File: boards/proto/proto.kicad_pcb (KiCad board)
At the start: 2 copper layers, 100 x 100 mm, 5 parts, among them J1 XBUS_02, J2 PIA_INT, J3 VIA_INT, J4 ACIA_INT

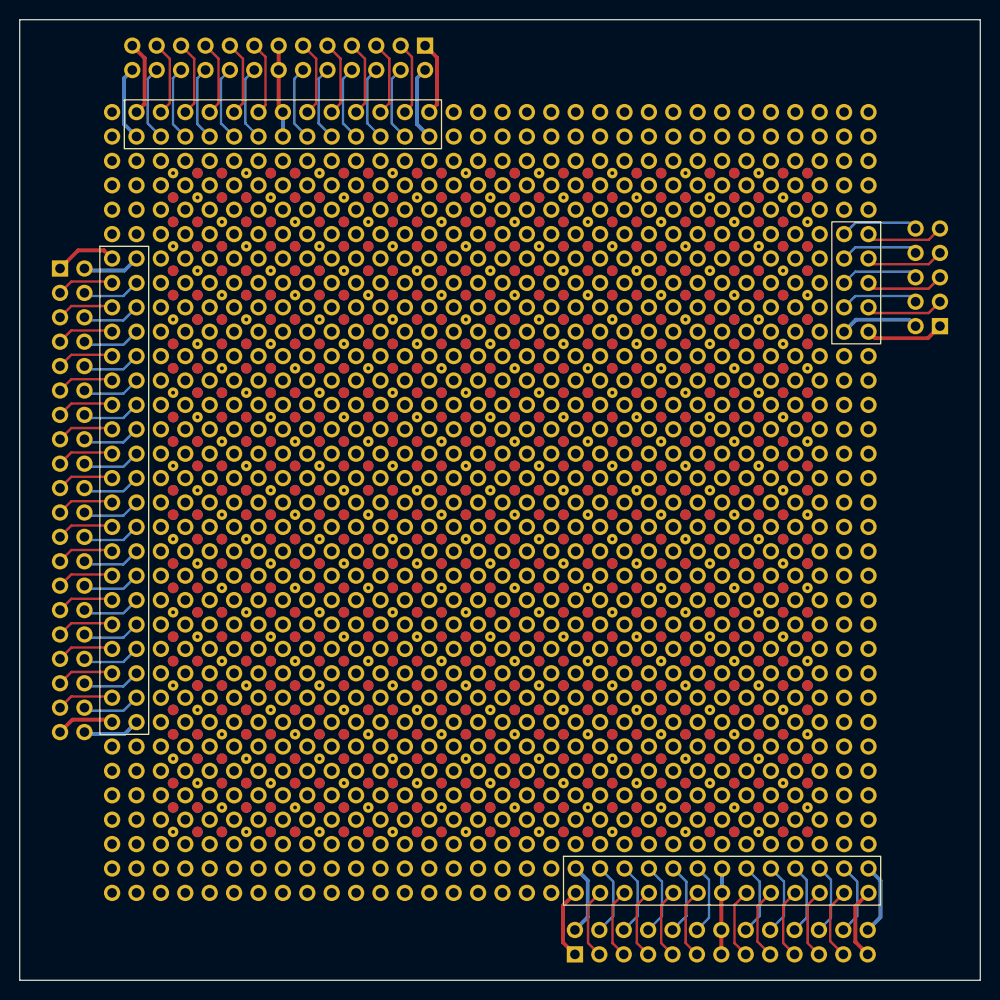
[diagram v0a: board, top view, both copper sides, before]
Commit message: Route PWR and GND traces from breakouts to proto rails.
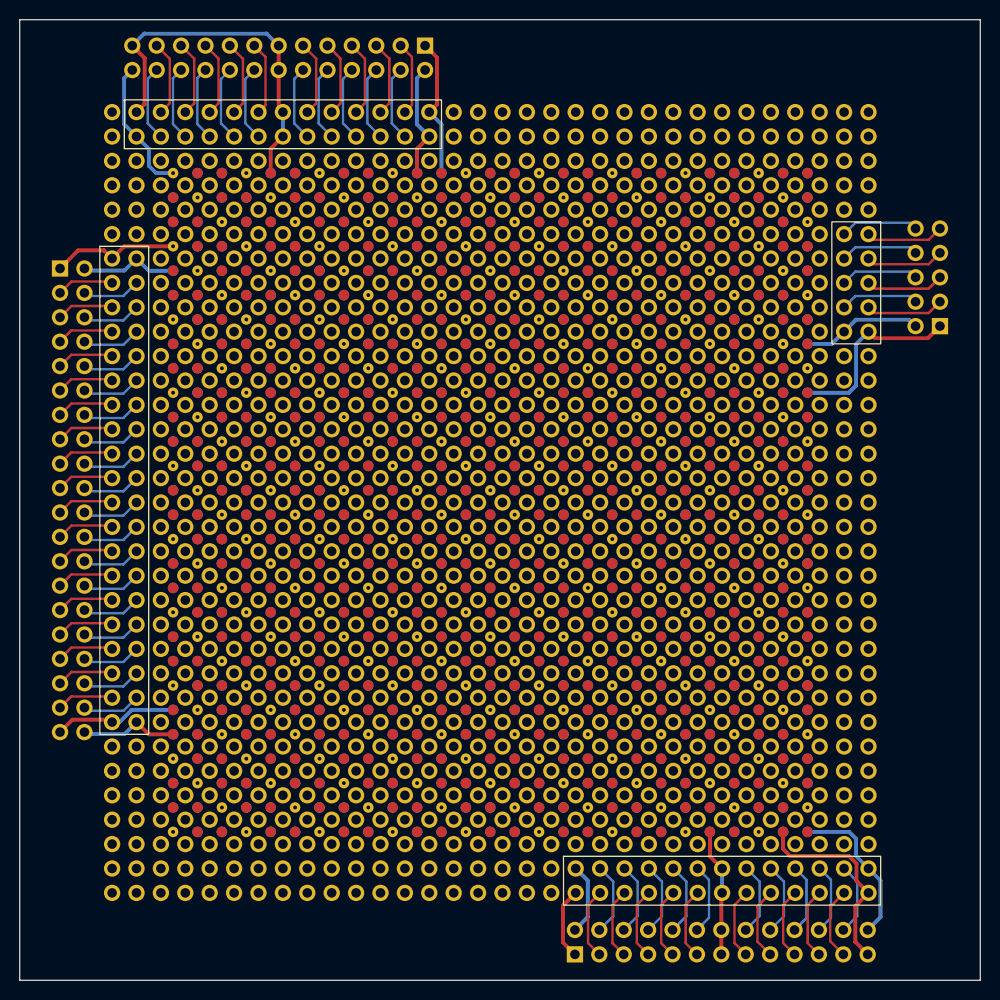
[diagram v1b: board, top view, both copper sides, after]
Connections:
- REF5 pad 1057: (no net) -> +5V
- REF5 pad 1058: (no net) -> +5V
- REF5 pad 1059: (no net) -> +5V
- REF5 pad 1060: (no net) -> +5V
- REF5 pad 1061: (no net) -> +5V
- REF5 pad 1062: (no net) -> +5V
- REF5 pad 1063: (no net) -> +5V
- REF5 pad 1064: (no net) -> +5V
- REF5 pad 1065: (no net) -> +5V
- REF5 pad 1066: (no net) -> +5V
- REF5 pad 1067: (no net) -> +5V
- REF5 pad 1068: (no net) -> +5V
- REF5 pad 1069: (no net) -> +5V
- REF5 pad 1070: (no net) -> +5V
- REF5 pad 1071: (no net) -> +5V
- REF5 pad 1072: (no net) -> +5V
- REF5 pad 1073: (no net) -> +5V
- REF5 pad 1074: (no net) -> +5V
- REF5 pad 1075: (no net) -> +5V
- REF5 pad 1076: (no net) -> +5V
- REF5 pad 1077: (no net) -> +5V
- REF5 pad 1078: (no net) -> +5V
- REF5 pad 1079: (no net) -> +5V
- REF5 pad 1080: (no net) -> +5V
- REF5 pad 1081: (no net) -> +5V
- REF5 pad 1082: (no net) -> +5V
- REF5 pad 1083: (no net) -> +5V
- REF5 pad 1084: (no net) -> +5V
- REF5 pad 1085: (no net) -> +5V
- REF5 pad 1086: (no net) -> +5V
- REF5 pad 1087: (no net) -> +5V
- REF5 pad 1088: (no net) -> +5V
- REF5 pad 1089: (no net) -> +5V
- REF5 pad 1090: (no net) -> +5V
- REF5 pad 1091: (no net) -> +5V
- REF5 pad 1092: (no net) -> +5V
- REF5 pad 1093: (no net) -> +5V
- REF5 pad 1094: (no net) -> +5V
- REF5 pad 1095: (no net) -> +5V
- REF5 pad 1096: (no net) -> +5V
- REF5 pad 1097: (no net) -> +5V
- REF5 pad 1098: (no net) -> +5V
- REF5 pad 1099: (no net) -> +5V
- REF5 pad 1100: (no net) -> +5V
- REF5 pad 1101: (no net) -> +5V
- REF5 pad 1102: (no net) -> +5V
- REF5 pad 1103: (no net) -> +5V
- REF5 pad 1104: (no net) -> +5V
- REF5 pad 1105: (no net) -> +5V
- REF5 pad 1106: (no net) -> +5V
- REF5 pad 1107: (no net) -> +5V
- REF5 pad 1108: (no net) -> +5V
- REF5 pad 1109: (no net) -> +5V
- REF5 pad 1110: (no net) -> +5V
- REF5 pad 1111: (no net) -> +5V
- REF5 pad 1112: (no net) -> +5V
- REF5 pad 1113: (no net) -> +5V
- REF5 pad 1114: (no net) -> +5V
- REF5 pad 1115: (no net) -> +5V
- REF5 pad 1116: (no net) -> +5V
- REF5 pad 1117: (no net) -> +5V
- REF5 pad 1118: (no net) -> +5V
- REF5 pad 1119: (no net) -> +5V
- REF5 pad 1120: (no net) -> +5V
- REF5 pad 1121: (no net) -> +5V
- REF5 pad 1122: (no net) -> +5V
- REF5 pad 1123: (no net) -> +5V
- REF5 pad 1124: (no net) -> +5V
- REF5 pad 1125: (no net) -> +5V
- REF5 pad 1126: (no net) -> +5V
- REF5 pad 1127: (no net) -> +5V
- REF5 pad 1128: (no net) -> +5V
- REF5 pad 1129: (no net) -> +5V
- REF5 pad 1130: (no net) -> +5V
- REF5 pad 1131: (no net) -> +5V
- REF5 pad 1132: (no net) -> +5V
- REF5 pad 1133: (no net) -> +5V
- REF5 pad 1134: (no net) -> +5V
- REF5 pad 1135: (no net) -> +5V
- REF5 pad 1136: (no net) -> +5V
- REF5 pad 1137: (no net) -> +5V
- REF5 pad 1138: (no net) -> +5V
- REF5 pad 1139: (no net) -> +5V
- REF5 pad 1140: (no net) -> +5V
- REF5 pad 1141: (no net) -> +5V
- REF5 pad 1142: (no net) -> +5V
- REF5 pad 1143: (no net) -> +5V
- REF5 pad 1144: (no net) -> +5V
- REF5 pad 1145: (no net) -> +5V
- REF5 pad 1146: (no net) -> +5V
- REF5 pad 1147: (no net) -> GND
- REF5 pad 1148: (no net) -> GND
- REF5 pad 1149: (no net) -> GND
- REF5 pad 1150: (no net) -> GND
- REF5 pad 1151: (no net) -> GND
- REF5 pad 1152: (no net) -> GND
- REF5 pad 1153: (no net) -> GND
- REF5 pad 1154: (no net) -> GND
- REF5 pad 1155: (no net) -> GND
- REF5 pad 1156: (no net) -> GND
- REF5 pad 1157: (no net) -> GND
- REF5 pad 1158: (no net) -> GND
- REF5 pad 1159: (no net) -> GND
- REF5 pad 1160: (no net) -> GND
- REF5 pad 1161: (no net) -> GND
- REF5 pad 1162: (no net) -> GND
- REF5 pad 1163: (no net) -> GND
- REF5 pad 1164: (no net) -> GND
- REF5 pad 1165: (no net) -> GND
- REF5 pad 1166: (no net) -> GND
- REF5 pad 1167: (no net) -> GND
- REF5 pad 1168: (no net) -> GND
- REF5 pad 1169: (no net) -> GND
- REF5 pad 1170: (no net) -> GND
- REF5 pad 1171: (no net) -> GND
- REF5 pad 1172: (no net) -> GND
- REF5 pad 1173: (no net) -> GND
- REF5 pad 1174: (no net) -> GND
- REF5 pad 1175: (no net) -> GND
- REF5 pad 1176: (no net) -> GND
- REF5 pad 1177: (no net) -> GND
- REF5 pad 1178: (no net) -> GND
- REF5 pad 1179: (no net) -> GND
- REF5 pad 1180: (no net) -> GND
- REF5 pad 1181: (no net) -> GND
- REF5 pad 1182: (no net) -> GND
- REF5 pad 1183: (no net) -> GND
- REF5 pad 1184: (no net) -> GND
- REF5 pad 1185: (no net) -> GND
- REF5 pad 1186: (no net) -> GND
- REF5 pad 1187: (no net) -> GND
- REF5 pad 1188: (no net) -> GND
- REF5 pad 1189: (no net) -> GND
- REF5 pad 1190: (no net) -> GND
- REF5 pad 1191: (no net) -> GND
- REF5 pad 1192: (no net) -> GND
- REF5 pad 1193: (no net) -> GND
- REF5 pad 1194: (no net) -> GND
- REF5 pad 1195: (no net) -> GND
- REF5 pad 1196: (no net) -> GND
- REF5 pad 1197: (no net) -> GND
- REF5 pad 1198: (no net) -> GND
- REF5 pad 1199: (no net) -> GND
- REF5 pad 1200: (no net) -> GND
- REF5 pad 1201: (no net) -> GND
- REF5 pad 1202: (no net) -> GND
- REF5 pad 1203: (no net) -> GND
- REF5 pad 1204: (no net) -> GND
- REF5 pad 1205: (no net) -> GND
- REF5 pad 1206: (no net) -> GND
- REF5 pad 1207: (no net) -> GND
- REF5 pad 1208: (no net) -> GND
- REF5 pad 1209: (no net) -> GND
- REF5 pad 1210: (no net) -> GND
- REF5 pad 1211: (no net) -> GND
- REF5 pad 1212: (no net) -> GND
- REF5 pad 1213: (no net) -> GND
- REF5 pad 1214: (no net) -> GND
- REF5 pad 1215: (no net) -> GND
- REF5 pad 1216: (no net) -> GND
- REF5 pad 1217: (no net) -> GND
- REF5 pad 1218: (no net) -> GND
- REF5 pad 1219: (no net) -> GND
- REF5 pad 1220: (no net) -> GND
- REF5 pad 1221: (no net) -> GND
- REF5 pad 1222: (no net) -> GND
- REF5 pad 1223: (no net) -> GND
- REF5 pad 1224: (no net) -> GND
- REF5 pad 1225: (no net) -> GND
- REF5 pad 1226: (no net) -> GND
- REF5 pad 1227: (no net) -> GND
- REF5 pad 1309: (no net) -> +5V
- REF5 pad 1310: (no net) -> +5V
- REF5 pad 1311: (no net) -> +5V
- REF5 pad 1312: (no net) -> +5V
- REF5 pad 1313: (no net) -> +5V
- REF5 pad 1314: (no net) -> +5V
- REF5 pad 1315: (no net) -> +5V
- REF5 pad 1316: (no net) -> +5V
- REF5 pad 1317: (no net) -> +5V
- REF5 pad 1318: (no net) -> +5V
- REF5 pad 1319: (no net) -> +5V
- REF5 pad 1320: (no net) -> +5V
- REF5 pad 1321: (no net) -> +5V
- REF5 pad 1322: (no net) -> +5V
- REF5 pad 1323: (no net) -> +5V
- REF5 pad 1324: (no net) -> +5V
- REF5 pad 1325: (no net) -> +5V
- REF5 pad 1326: (no net) -> +5V
- REF5 pad 1327: (no net) -> +5V
- REF5 pad 1328: (no net) -> +5V
- REF5 pad 1329: (no net) -> +5V
- REF5 pad 1330: (no net) -> +5V
- REF5 pad 1331: (no net) -> +5V
- REF5 pad 1332: (no net) -> +5V
- REF5 pad 1333: (no net) -> +5V
- REF5 pad 1334: (no net) -> +5V
- REF5 pad 1335: (no net) -> +5V
- REF5 pad 1336: (no net) -> +5V
- REF5 pad 1337: (no net) -> +5V
- REF5 pad 1338: (no net) -> +5V
- REF5 pad 1339: (no net) -> +5V
- REF5 pad 1340: (no net) -> +5V
- REF5 pad 1341: (no net) -> +5V
- REF5 pad 1342: (no net) -> +5V
- REF5 pad 1343: (no net) -> +5V
- REF5 pad 1344: (no net) -> +5V
- REF5 pad 1345: (no net) -> +5V
- REF5 pad 1346: (no net) -> +5V
- REF5 pad 1347: (no net) -> +5V
- REF5 pad 1348: (no net) -> +5V
- REF5 pad 1349: (no net) -> +5V
- REF5 pad 1350: (no net) -> +5V
- REF5 pad 1351: (no net) -> +5V
- REF5 pad 1352: (no net) -> +5V
- REF5 pad 1353: (no net) -> +5V
- REF5 pad 1354: (no net) -> +5V
- REF5 pad 1355: (no net) -> +5V
- REF5 pad 1356: (no net) -> +5V
- REF5 pad 1357: (no net) -> +5V
- REF5 pad 1358: (no net) -> +5V
- REF5 pad 1359: (no net) -> +5V
- REF5 pad 1360: (no net) -> +5V
- REF5 pad 1361: (no net) -> +5V
- REF5 pad 1362: (no net) -> +5V
- REF5 pad 1363: (no net) -> +5V
- REF5 pad 1364: (no net) -> +5V
- REF5 pad 1365: (no net) -> +5V
- REF5 pad 1366: (no net) -> +5V
- REF5 pad 1367: (no net) -> +5V
- REF5 pad 1368: (no net) -> +5V
- REF5 pad 1369: (no net) -> +5V
- REF5 pad 1370: (no net) -> +5V
- REF5 pad 1371: (no net) -> +5V
- REF5 pad 1372: (no net) -> +5V
- REF5 pad 1373: (no net) -> +5V
- REF5 pad 1374: (no net) -> +5V
- REF5 pad 1375: (no net) -> +5V
- REF5 pad 1376: (no net) -> +5V
- REF5 pad 1377: (no net) -> +5V
- REF5 pad 1378: (no net) -> +5V
- REF5 pad 1379: (no net) -> +5V
- REF5 pad 1380: (no net) -> +5V
- REF5 pad 1381: (no net) -> +5V
- REF5 pad 1382: (no net) -> +5V
- REF5 pad 1383: (no net) -> +5V
- REF5 pad 1384: (no net) -> +5V
- REF5 pad 1385: (no net) -> +5V
- REF5 pad 1386: (no net) -> +5V
- REF5 pad 1387: (no net) -> +5V
- REF5 pad 1388: (no net) -> +5V
- REF5 pad 1389: (no net) -> +5V
- REF5 pad 1390: (no net) -> +5V
- REF5 pad 1391: (no net) -> +5V
- REF5 pad 1392: (no net) -> +5V
- REF5 pad 1393: (no net) -> +5V
- REF5 pad 1394: (no net) -> +5V
- REF5 pad 1395: (no net) -> +5V
- REF5 pad 1396: (no net) -> +5V
- REF5 pad 1397: (no net) -> +5V
- REF5 pad 1398: (no net) -> +5V
- REF5 pad 1399: (no net) -> +5V
- REF5 pad 1400: (no net) -> +5V
- REF5 pad 1401: (no net) -> +5V
- REF5 pad 1402: (no net) -> +5V
- REF5 pad 1403: (no net) -> +5V
- REF5 pad 1404: (no net) -> +5V
- REF5 pad 1405: (no net) -> +5V
- REF5 pad 1406: (no net) -> +5V
- REF5 pad 1407: (no net) -> +5V
- REF5 pad 1408: (no net) -> +5V
- REF5 pad 1409: (no net) -> +5V
- REF5 pad 1410: (no net) -> +5V
- REF5 pad 1411: (no net) -> +5V
- REF5 pad 1412: (no net) -> +5V
- REF5 pad 1413: (no net) -> +5V
- REF5 pad 1414: (no net) -> +5V
- REF5 pad 1415: (no net) -> +5V
- REF5 pad 1416: (no net) -> +5V
- REF5 pad 1417: (no net) -> +5V
- REF5 pad 1418: (no net) -> +5V
- REF5 pad 1419: (no net) -> +5V
- REF5 pad 1420: (no net) -> +5V
- REF5 pad 1421: (no net) -> +5V
- REF5 pad 1422: (no net) -> +5V
- REF5 pad 1423: (no net) -> +5V
- REF5 pad 1424: (no net) -> +5V
- REF5 pad 1425: (no net) -> +5V
- REF5 pad 1426: (no net) -> +5V
- REF5 pad 1427: (no net) -> +5V
- REF5 pad 1428: (no net) -> +5V
- REF5 pad 1429: (no net) -> +5V
- REF5 pad 1430: (no net) -> +5V
- REF5 pad 1431: (no net) -> +5V
- REF5 pad 1432: (no net) -> +5V
- REF5 pad 1433: (no net) -> +5V
- REF5 pad 1434: (no net) -> +5V
- REF5 pad 1435: (no net) -> +5V
- REF5 pad 1436: (no net) -> +5V
- REF5 pad 1437: (no net) -> +5V
- REF5 pad 1438: (no net) -> +5V
- REF5 pad 1439: (no net) -> +5V
- REF5 pad 1440: (no net) -> +5V
- REF5 pad 1441: (no net) -> +5V
- REF5 pad 1442: (no net) -> +5V
- REF5 pad 1443: (no net) -> +5V
- REF5 pad 1444: (no net) -> +5V
- REF5 pad 1445: (no net) -> +5V
- REF5 pad 1446: (no net) -> +5V
- REF5 pad 1447: (no net) -> +5V
- REF5 pad 1448: (no net) -> +5V
- REF5 pad 1449: (no net) -> +5V
- REF5 pad 1450: (no net) -> +5V
- REF5 pad 1451: (no net) -> +5V
- REF5 pad 1452: (no net) -> +5V
- REF5 pad 1453: (no net) -> +5V
- REF5 pad 1454: (no net) -> +5V
- REF5 pad 1455: (no net) -> +5V
- REF5 pad 1456: (no net) -> +5V
- REF5 pad 1457: (no net) -> +5V
- REF5 pad 1458: (no net) -> +5V
- REF5 pad 1459: (no net) -> +5V
- REF5 pad 1460: (no net) -> +5V
- REF5 pad 1461: (no net) -> +5V
- REF5 pad 1462: (no net) -> +5V
- REF5 pad 1463: (no net) -> +5V
- REF5 pad 1464: (no net) -> +5V
- REF5 pad 1465: (no net) -> +5V
- REF5 pad 1466: (no net) -> +5V
- REF5 pad 1467: (no net) -> +5V
- REF5 pad 1468: (no net) -> +5V
- REF5 pad 1469: (no net) -> +5V
- REF5 pad 1470: (no net) -> +5V
- REF5 pad 1471: (no net) -> +5V
- REF5 pad 1472: (no net) -> +5V
- REF5 pad 1473: (no net) -> +5V
- REF5 pad 1474: (no net) -> +5V
- REF5 pad 1475: (no net) -> +5V
- REF5 pad 1476: (no net) -> +5V
- REF5 pad 1477: (no net) -> +5V
- REF5 pad 1478: (no net) -> +5V
- REF5 pad 1479: (no net) -> +5V
- REF5 pad 1480: (no net) -> +5V
- REF5 pad 1481: (no net) -> +5V
- REF5 pad 1482: (no net) -> +5V
- REF5 pad 1483: (no net) -> +5V
- REF5 pad 1484: (no net) -> +5V
- REF5 pad 1485: (no net) -> +5V
- REF5 pad 1486: (no net) -> +5V
- REF5 pad 1487: (no net) -> +5V
- REF5 pad 1488: (no net) -> +5V
- REF5 pad 1489: (no net) -> +5V
- REF5 pad 1490: (no net) -> +5V
- REF5 pad 1491: (no net) -> +5V
- REF5 pad 1492: (no net) -> +5V
- REF5 pad 1493: (no net) -> +5V
- REF5 pad 1494: (no net) -> +5V
- REF5 pad 1495: (no net) -> +5V
- REF5 pad 1496: (no net) -> +5V
- REF5 pad 1497: (no net) -> +5V
- REF5 pad 1498: (no net) -> +5V
- REF5 pad 1499: (no net) -> +5V
- REF5 pad 1500: (no net) -> +5V
- REF5 pad 1501: (no net) -> +5V
- REF5 pad 1502: (no net) -> +5V
- REF5 pad 1503: (no net) -> +5V
- REF5 pad 1504: (no net) -> +5V
- REF5 pad 1505: (no net) -> +5V
- REF5 pad 1506: (no net) -> +5V
- REF5 pad 1507: (no net) -> +5V
- REF5 pad 1508: (no net) -> +5V
- REF5 pad 1509: (no net) -> +5V
- REF5 pad 1510: (no net) -> +5V
- REF5 pad 1511: (no net) -> +5V
- REF5 pad 1512: (no net) -> +5V
- REF5 pad 1513: (no net) -> +5V
- REF5 pad 1514: (no net) -> +5V
- REF5 pad 1515: (no net) -> +5V
- REF5 pad 1516: (no net) -> +5V
- REF5 pad 1517: (no net) -> +5V
- REF5 pad 1518: (no net) -> +5V
- REF5 pad 1519: (no net) -> +5V
- REF5 pad 1520: (no net) -> +5V
- REF5 pad 1521: (no net) -> +5V
- REF5 pad 1522: (no net) -> +5V
- REF5 pad 1523: (no net) -> +5V
- REF5 pad 1524: (no net) -> +5V
- REF5 pad 1525: (no net) -> +5V
- REF5 pad 1526: (no net) -> +5V
- REF5 pad 1527: (no net) -> +5V
- REF5 pad 1528: (no net) -> +5V
- REF5 pad 1529: (no net) -> +5V
- REF5 pad 1530: (no net) -> +5V
- REF5 pad 1531: (no net) -> +5V
- REF5 pad 1532: (no net) -> +5V
- REF5 pad 1533: (no net) -> +5V
- REF5 pad 1534: (no net) -> +5V
- REF5 pad 1535: (no net) -> +5V
- REF5 pad 1536: (no net) -> +5V
- REF5 pad 1537: (no net) -> +5V
- REF5 pad 1538: (no net) -> +5V
- REF5 pad 1539: (no net) -> +5V
- REF5 pad 1540: (no net) -> +5V
- REF5 pad 1541: (no net) -> +5V
- REF5 pad 1542: (no net) -> +5V
- REF5 pad 1543: (no net) -> +5V
- REF5 pad 1544: (no net) -> +5V
- REF5 pad 1545: (no net) -> +5V
- REF5 pad 1546: (no net) -> +5V
- REF5 pad 1547: (no net) -> +5V
- REF5 pad 1548: (no net) -> +5V
- REF5 pad 1549: (no net) -> +5V
- REF5 pad 1550: (no net) -> +5V
- REF5 pad 1551: (no net) -> +5V
- REF5 pad 1552: (no net) -> +5V
- REF5 pad 1553: (no net) -> +5V
- REF5 pad 1554: (no net) -> +5V
- REF5 pad 1555: (no net) -> +5V
- REF5 pad 1556: (no net) -> +5V
- REF5 pad 1557: (no net) -> +5V
- REF5 pad 1558: (no net) -> +5V
- REF5 pad 1559: (no net) -> +5V
- REF5 pad 1560: (no net) -> +5V
- REF5 pad 1561: (no net) -> +5V
- REF5 pad 1562: (no net) -> +5V
- REF5 pad 1563: (no net) -> +5V
- REF5 pad 1564: (no net) -> +5V
- REF5 pad 1565: (no net) -> +5V
- REF5 pad 1566: (no net) -> +5V
- REF5 pad 1567: (no net) -> +5V
- REF5 pad 1568: (no net) -> +5V
- REF5 pad 1569: (no net) -> +5V
- REF5 pad 1570: (no net) -> +5V
- REF5 pad 1571: (no net) -> +5V
- REF5 pad 1572: (no net) -> +5V
- REF5 pad 1573: (no net) -> +5V
- REF5 pad 1574: (no net) -> +5V
- REF5 pad 1575: (no net) -> +5V
- REF5 pad 1576: (no net) -> +5V
- REF5 pad 1577: (no net) -> +5V
- REF5 pad 1578: (no net) -> +5V
- REF5 pad 1579: (no net) -> +5V
- REF5 pad 1580: (no net) -> +5V
- REF5 pad 1581: (no net) -> +5V
- REF5 pad 1582: (no net) -> +5V
- REF5 pad 1583: (no net) -> +5V
- REF5 pad 1584: (no net) -> +5V
- REF5 pad 1585: (no net) -> +5V
- REF5 pad 1586: (no net) -> +5V
- REF5 pad 1587: (no net) -> +5V
- REF5 pad 1588: (no net) -> +5V
- REF5 pad 1589: (no net) -> +5V
- REF5 pad 1590: (no net) -> +5V
- REF5 pad 1591: (no net) -> +5V
- REF5 pad 1592: (no net) -> +5V
- REF5 pad 1593: (no net) -> +5V
- REF5 pad 1594: (no net) -> +5V
- REF5 pad 1595: (no net) -> +5V
- REF5 pad 1596: (no net) -> +5V
- REF5 pad 1597: (no net) -> +5V
- REF5 pad 1598: (no net) -> +5V
- REF5 pad 1599: (no net) -> +5V
- REF5 pad 1600: (no net) -> +5V
- REF5 pad 1601: (no net) -> +5V
- REF5 pad 1602: (no net) -> +5V
- REF5 pad 1603: (no net) -> +5V
- REF5 pad 1604: (no net) -> +5V
- REF5 pad 1605: (no net) -> +5V
- REF5 pad 1606: (no net) -> +5V
- REF5 pad 1607: (no net) -> +5V
- REF5 pad 1608: (no net) -> +5V
- REF5 pad 1609: (no net) -> +5V
- REF5 pad 1610: (no net) -> +5V
- REF5 pad 1611: (no net) -> +5V
- REF5 pad 1612: (no net) -> +5V
- REF5 pad 1613: (no net) -> +5V
- REF5 pad 1614: (no net) -> +5V
- REF5 pad 1615: (no net) -> +5V
- REF5 pad 1616: (no net) -> +5V
- REF5 pad 1617: (no net) -> +5V
- REF5 pad 1618: (no net) -> +5V
- REF5 pad 1619: (no net) -> +5V
- REF5 pad 1620: (no net) -> +5V
- REF5 pad 1621: (no net) -> +5V
- REF5 pad 1622: (no net) -> +5V
- REF5 pad 1623: (no net) -> +5V
- REF5 pad 1624: (no net) -> +5V
- REF5 pad 1625: (no net) -> +5V
- REF5 pad 1626: (no net) -> +5V
- REF5 pad 1627: (no net) -> +5V
- REF5 pad 1628: (no net) -> +5V
- REF5 pad 1629: (no net) -> +5V
- REF5 pad 1630: (no net) -> +5V
- REF5 pad 1631: (no net) -> +5V
- REF5 pad 1632: (no net) -> +5V
- REF5 pad 1633: (no net) -> +5V
- REF5 pad 1634: (no net) -> +5V
- REF5 pad 1635: (no net) -> +5V
- REF5 pad 1636: (no net) -> +5V
- REF5 pad 1637: (no net) -> +5V
- REF5 pad 1638: (no net) -> +5V
- REF5 pad 1639: (no net) -> +5V
- REF5 pad 1640: (no net) -> +5V
- REF5 pad 1641: (no net) -> +5V
- REF5 pad 1642: (no net) -> +5V
- REF5 pad 1643: (no net) -> +5V
- REF5 pad 1644: (no net) -> +5V
- REF5 pad 1645: (no net) -> +5V
- REF5 pad 1646: (no net) -> +5V
- REF5 pad 1647: (no net) -> +5V
- REF5 pad 1648: (no net) -> +5V
- REF5 pad 1649: (no net) -> +5V
- REF5 pad 1650: (no net) -> +5V
- REF5 pad 1651: (no net) -> GND
- REF5 pad 1652: (no net) -> GND
- REF5 pad 1653: (no net) -> GND
- REF5 pad 1654: (no net) -> GND
- REF5 pad 1655: (no net) -> GND
- REF5 pad 1656: (no net) -> GND
- REF5 pad 1657: (no net) -> GND
- REF5 pad 1658: (no net) -> GND
- REF5 pad 1659: (no net) -> GND
- REF5 pad 1660: (no net) -> GND
- REF5 pad 1661: (no net) -> GND
- REF5 pad 1662: (no net) -> GND
- REF5 pad 1663: (no net) -> GND
- REF5 pad 1664: (no net) -> GND
- REF5 pad 1665: (no net) -> GND
- REF5 pad 1666: (no net) -> GND
- REF5 pad 1667: (no net) -> GND
- REF5 pad 1668: (no net) -> GND
- REF5 pad 1669: (no net) -> GND
- REF5 pad 1670: (no net) -> GND
- REF5 pad 1671: (no net) -> GND
- REF5 pad 1672: (no net) -> GND
- REF5 pad 1673: (no net) -> GND
- REF5 pad 1674: (no net) -> GND
- REF5 pad 1675: (no net) -> GND
- REF5 pad 1676: (no net) -> GND
- REF5 pad 1677: (no net) -> GND
- REF5 pad 1678: (no net) -> GND
- REF5 pad 1679: (no net) -> GND
- REF5 pad 1680: (no net) -> GND
- REF5 pad 1681: (no net) -> GND
- REF5 pad 1682: (no net) -> GND
- REF5 pad 1683: (no net) -> GND
- REF5 pad 1684: (no net) -> GND
- REF5 pad 1685: (no net) -> GND
- REF5 pad 1686: (no net) -> GND
- REF5 pad 1687: (no net) -> GND
- REF5 pad 1688: (no net) -> GND
- REF5 pad 1689: (no net) -> GND
- REF5 pad 1690: (no net) -> GND
- REF5 pad 1691: (no net) -> GND
- REF5 pad 1692: (no net) -> GND
- REF5 pad 1693: (no net) -> GND
- REF5 pad 1694: (no net) -> GND
- REF5 pad 1695: (no net) -> GND
- REF5 pad 1696: (no net) -> GND
- REF5 pad 1697: (no net) -> GND
- REF5 pad 1698: (no net) -> GND
- REF5 pad 1699: (no net) -> GND
- REF5 pad 1700: (no net) -> GND
- REF5 pad 1701: (no net) -> GND
- REF5 pad 1702: (no net) -> GND
- REF5 pad 1703: (no net) -> GND
- REF5 pad 1704: (no net) -> GND
- REF5 pad 1705: (no net) -> GND
- REF5 pad 1706: (no net) -> GND
- REF5 pad 1707: (no net) -> GND
- REF5 pad 1708: (no net) -> GND
- REF5 pad 1709: (no net) -> GND
- REF5 pad 1710: (no net) -> GND
- REF5 pad 1711: (no net) -> GND
- REF5 pad 1712: (no net) -> GND
- REF5 pad 1713: (no net) -> GND
- REF5 pad 1714: (no net) -> GND
- REF5 pad 1715: (no net) -> GND
- REF5 pad 1716: (no net) -> GND
- REF5 pad 1717: (no net) -> GND
- REF5 pad 1718: (no net) -> GND
- REF5 pad 1719: (no net) -> GND
- REF5 pad 1720: (no net) -> GND
- REF5 pad 1721: (no net) -> GND
- REF5 pad 1722: (no net) -> GND
- REF5 pad 1723: (no net) -> GND
- REF5 pad 1724: (no net) -> GND
- REF5 pad 1725: (no net) -> GND
- REF5 pad 1726: (no net) -> GND
- REF5 pad 1727: (no net) -> GND
- REF5 pad 1728: (no net) -> GND
- REF5 pad 1729: (no net) -> GND
- REF5 pad 1730: (no net) -> GND
- REF5 pad 1731: (no net) -> GND
- REF5 pad 1732: (no net) -> GND
- REF5 pad 1733: (no net) -> GND
- REF5 pad 1734: (no net) -> GND
- REF5 pad 1735: (no net) -> GND
- REF5 pad 1736: (no net) -> GND
- REF5 pad 1737: (no net) -> GND
- REF5 pad 1738: (no net) -> GND
- REF5 pad 1739: (no net) -> GND
- REF5 pad 1740: (no net) -> GND
- REF5 pad 1741: (no net) -> GND
- REF5 pad 1742: (no net) -> GND
- REF5 pad 1743: (no net) -> GND
- REF5 pad 1744: (no net) -> GND
- REF5 pad 1745: (no net) -> GND
- REF5 pad 1746: (no net) -> GND
- REF5 pad 1747: (no net) -> GND
- REF5 pad 1748: (no net) -> GND
- REF5 pad 1749: (no net) -> GND
- REF5 pad 1750: (no net) -> GND
- REF5 pad 1751: (no net) -> GND
- REF5 pad 1752: (no net) -> GND
- REF5 pad 1753: (no net) -> GND
- REF5 pad 1754: (no net) -> GND
- REF5 pad 1755: (no net) -> GND
- REF5 pad 1756: (no net) -> GND
- REF5 pad 1757: (no net) -> GND
- REF5 pad 1758: (no net) -> GND
- REF5 pad 1759: (no net) -> GND
- REF5 pad 1760: (no net) -> GND
- REF5 pad 1761: (no net) -> GND
- REF5 pad 1762: (no net) -> GND
- REF5 pad 1763: (no net) -> GND
- REF5 pad 1764: (no net) -> GND
- REF5 pad 1765: (no net) -> GND
- REF5 pad 1766: (no net) -> GND
- REF5 pad 1767: (no net) -> GND
- REF5 pad 1768: (no net) -> GND
- REF5 pad 1769: (no net) -> GND
- REF5 pad 1770: (no net) -> GND
- REF5 pad 1771: (no net) -> GND
- REF5 pad 1772: (no net) -> GND
- REF5 pad 1773: (no net) -> GND
- REF5 pad 1774: (no net) -> GND
- REF5 pad 1775: (no net) -> GND
- REF5 pad 1776: (no net) -> GND
- REF5 pad 1777: (no net) -> GND
- REF5 pad 1778: (no net) -> GND
- REF5 pad 1779: (no net) -> GND
- REF5 pad 1780: (no net) -> GND
- REF5 pad 1781: (no net) -> GND
- REF5 pad 1782: (no net) -> GND
- REF5 pad 1783: (no net) -> GND
- REF5 pad 1784: (no net) -> GND
- REF5 pad 1785: (no net) -> GND
- REF5 pad 1786: (no net) -> GND
- REF5 pad 1787: (no net) -> GND
- REF5 pad 1788: (no net) -> GND
- REF5 pad 1789: (no net) -> GND
- REF5 pad 1790: (no net) -> GND
- REF5 pad 1791: (no net) -> GND
- REF5 pad 1792: (no net) -> GND
- REF5 pad 1793: (no net) -> GND
- REF5 pad 1794: (no net) -> GND
- REF5 pad 1795: (no net) -> GND
- REF5 pad 1796: (no net) -> GND
- REF5 pad 1797: (no net) -> GND
- REF5 pad 1798: (no net) -> GND
- REF5 pad 1799: (no net) -> GND
- REF5 pad 1800: (no net) -> GND
- REF5 pad 1801: (no net) -> GND
- REF5 pad 1802: (no net) -> GND
- REF5 pad 1803: (no net) -> GND
- REF5 pad 1804: (no net) -> GND
- REF5 pad 1805: (no net) -> GND
- REF5 pad 1806: (no net) -> GND
- REF5 pad 1807: (no net) -> GND
- REF5 pad 1808: (no net) -> GND
- REF5 pad 1809: (no net) -> GND
- REF5 pad 1810: (no net) -> GND
- REF5 pad 1811: (no net) -> GND
- REF5 pad 1812: (no net) -> GND
- REF5 pad 1813: (no net) -> GND
- REF5 pad 1814: (no net) -> GND
- REF5 pad 1815: (no net) -> GND
- REF5 pad 1816: (no net) -> GND
- REF5 pad 1817: (no net) -> GND
- REF5 pad 1818: (no net) -> GND
- REF5 pad 1819: (no net) -> GND
- REF5 pad 1820: (no net) -> GND
- REF5 pad 1821: (no net) -> GND
- REF5 pad 1822: (no net) -> GND
- REF5 pad 1823: (no net) -> GND
- REF5 pad 1824: (no net) -> GND
- REF5 pad 1825: (no net) -> GND
- REF5 pad 1826: (no net) -> GND
- REF5 pad 1827: (no net) -> GND
- REF5 pad 1828: (no net) -> GND
- REF5 pad 1829: (no net) -> GND
- REF5 pad 1830: (no net) -> GND
- REF5 pad 1831: (no net) -> GND
- REF5 pad 1832: (no net) -> GND
- REF5 pad 1833: (no net) -> GND
- REF5 pad 1834: (no net) -> GND
- REF5 pad 1835: (no net) -> GND
- REF5 pad 1836: (no net) -> GND
- REF5 pad 1837: (no net) -> GND
- REF5 pad 1838: (no net) -> GND
- REF5 pad 1839: (no net) -> GND
- REF5 pad 1840: (no net) -> GND
- REF5 pad 1841: (no net) -> GND
- REF5 pad 1842: (no net) -> GND
- REF5 pad 1843: (no net) -> GND
- REF5 pad 1844: (no net) -> GND
- REF5 pad 1845: (no net) -> GND
- REF5 pad 1846: (no net) -> GND
- REF5 pad 1847: (no net) -> GND
- REF5 pad 1848: (no net) -> GND
- REF5 pad 1849: (no net) -> GND
- REF5 pad 1850: (no net) -> GND
- REF5 pad 1851: (no net) -> GND
- REF5 pad 1852: (no net) -> GND
- REF5 pad 1853: (no net) -> GND
- REF5 pad 1854: (no net) -> GND
- REF5 pad 1855: (no net) -> GND
- REF5 pad 1856: (no net) -> GND
- REF5 pad 1857: (no net) -> GND
- REF5 pad 1858: (no net) -> GND
- REF5 pad 1859: (no net) -> GND
- REF5 pad 1860: (no net) -> GND
- REF5 pad 1861: (no net) -> GND
- REF5 pad 1862: (no net) -> GND
- REF5 pad 1863: (no net) -> GND
- REF5 pad 1864: (no net) -> GND
- REF5 pad 1865: (no net) -> GND
- REF5 pad 1866: (no net) -> GND
- REF5 pad 1867: (no net) -> GND
- REF5 pad 1868: (no net) -> GND
- REF5 pad 1869: (no net) -> GND
- REF5 pad 1870: (no net) -> GND
- REF5 pad 1871: (no net) -> GND
- REF5 pad 1872: (no net) -> GND
- REF5 pad 1873: (no net) -> GND
- REF5 pad 1874: (no net) -> GND
- REF5 pad 1875: (no net) -> GND
- REF5 pad 1876: (no net) -> GND
- REF5 pad 1877: (no net) -> GND
- REF5 pad 1878: (no net) -> GND
- REF5 pad 1879: (no net) -> GND
- REF5 pad 1880: (no net) -> GND
- REF5 pad 1881: (no net) -> GND
- REF5 pad 1882: (no net) -> GND
- REF5 pad 1883: (no net) -> GND
- REF5 pad 1884: (no net) -> GND
- REF5 pad 1885: (no net) -> GND
- REF5 pad 1886: (no net) -> GND
- REF5 pad 1887: (no net) -> GND
- REF5 pad 1888: (no net) -> GND
- REF5 pad 1889: (no net) -> GND
- REF5 pad 1890: (no net) -> GND
- REF5 pad 1891: (no net) -> GND
- REF5 pad 1892: (no net) -> GND
- REF5 pad 1893: (no net) -> GND
- REF5 pad 1894: (no net) -> GND
- REF5 pad 1895: (no net) -> GND
- REF5 pad 1896: (no net) -> GND
- REF5 pad 1897: (no net) -> GND
- REF5 pad 1898: (no net) -> GND
- REF5 pad 1899: (no net) -> GND
- REF5 pad 1900: (no net) -> GND
- REF5 pad 1901: (no net) -> GND
- REF5 pad 1902: (no net) -> GND
- REF5 pad 1903: (no net) -> GND
- REF5 pad 1904: (no net) -> GND
- REF5 pad 1905: (no net) -> GND
- REF5 pad 1906: (no net) -> GND
- REF5 pad 1907: (no net) -> GND
- REF5 pad 1908: (no net) -> GND
- REF5 pad 1909: (no net) -> GND
- REF5 pad 1910: (no net) -> GND
- REF5 pad 1911: (no net) -> GND
- REF5 pad 1912: (no net) -> GND
- REF5 pad 1913: (no net) -> GND
- REF5 pad 1914: (no net) -> GND
- REF5 pad 1915: (no net) -> GND
- REF5 pad 1916: (no net) -> GND
- REF5 pad 1917: (no net) -> GND
- REF5 pad 1918: (no net) -> GND
- REF5 pad 1919: (no net) -> GND
- REF5 pad 1920: (no net) -> GND
- REF5 pad 1921: (no net) -> GND
- REF5 pad 1922: (no net) -> GND
- REF5 pad 1923: (no net) -> GND
- REF5 pad 1924: (no net) -> GND
- REF5 pad 1925: (no net) -> GND
- REF5 pad 1926: (no net) -> GND
- REF5 pad 1927: (no net) -> GND
- REF5 pad 1928: (no net) -> GND
- REF5 pad 1929: (no net) -> GND
- REF5 pad 1930: (no net) -> GND
- REF5 pad 1931: (no net) -> GND
- REF5 pad 1932: (no net) -> GND
- REF5 pad 1933: (no net) -> GND
- REF5 pad 1934: (no net) -> GND
- REF5 pad 1935: (no net) -> GND
- REF5 pad 1936: (no net) -> GND
- REF5 pad 1937: (no net) -> GND
- REF5 pad 1938: (no net) -> GND
- REF5 pad 1939: (no net) -> GND
- REF5 pad 1940: (no net) -> GND
- REF5 pad 1941: (no net) -> GND
- REF5 pad 1942: (no net) -> GND
- REF5 pad 1943: (no net) -> GND
- REF5 pad 1944: (no net) -> GND
- REF5 pad 1945: (no net) -> GND
- REF5 pad 1946: (no net) -> GND
- REF5 pad 1947: (no net) -> GND
- REF5 pad 1948: (no net) -> GND
- REF5 pad 1949: (no net) -> GND
- REF5 pad 1950: (no net) -> GND
- REF5 pad 1951: (no net) -> GND
- REF5 pad 1952: (no net) -> GND
- REF5 pad 1953: (no net) -> GND
- REF5 pad 1954: (no net) -> GND
- REF5 pad 1955: (no net) -> GND
- REF5 pad 1956: (no net) -> GND
- REF5 pad 1957: (no net) -> GND
- REF5 pad 1958: (no net) -> GND
- REF5 pad 1959: (no net) -> GND
- REF5 pad 1960: (no net) -> GND
- REF5 pad 1961: (no net) -> GND
- REF5 pad 1962: (no net) -> GND
- REF5 pad 1963: (no net) -> GND
- REF5 pad 1964: (no net) -> GND
- REF5 pad 1965: (no net) -> GND
- REF5 pad 1966: (no net) -> GND
- REF5 pad 1967: (no net) -> GND
- REF5 pad 1968: (no net) -> GND
- REF5 pad 1969: (no net) -> GND
- REF5 pad 1970: (no net) -> GND
- REF5 pad 1971: (no net) -> GND
- REF5 pad 1972: (no net) -> GND
- REF5 pad 1973: (no net) -> GND
- REF5 pad 1974: (no net) -> GND
- REF5 pad 1975: (no net) -> GND
- REF5 pad 1976: (no net) -> GND
- REF5 pad 1977: (no net) -> GND
- REF5 pad 1978: (no net) -> GND
- REF5 pad 1979: (no net) -> GND
- REF5 pad 1980: (no net) -> GND
- REF5 pad 1981: (no net) -> GND
- REF5 pad 1982: (no net) -> GND
- REF5 pad 1983: (no net) -> GND
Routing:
- net GND: track 69.5 -> 128.0 mm
- net +5V: track 51.3 -> 96.3 mm

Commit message: Completely routed design, except for user rail.
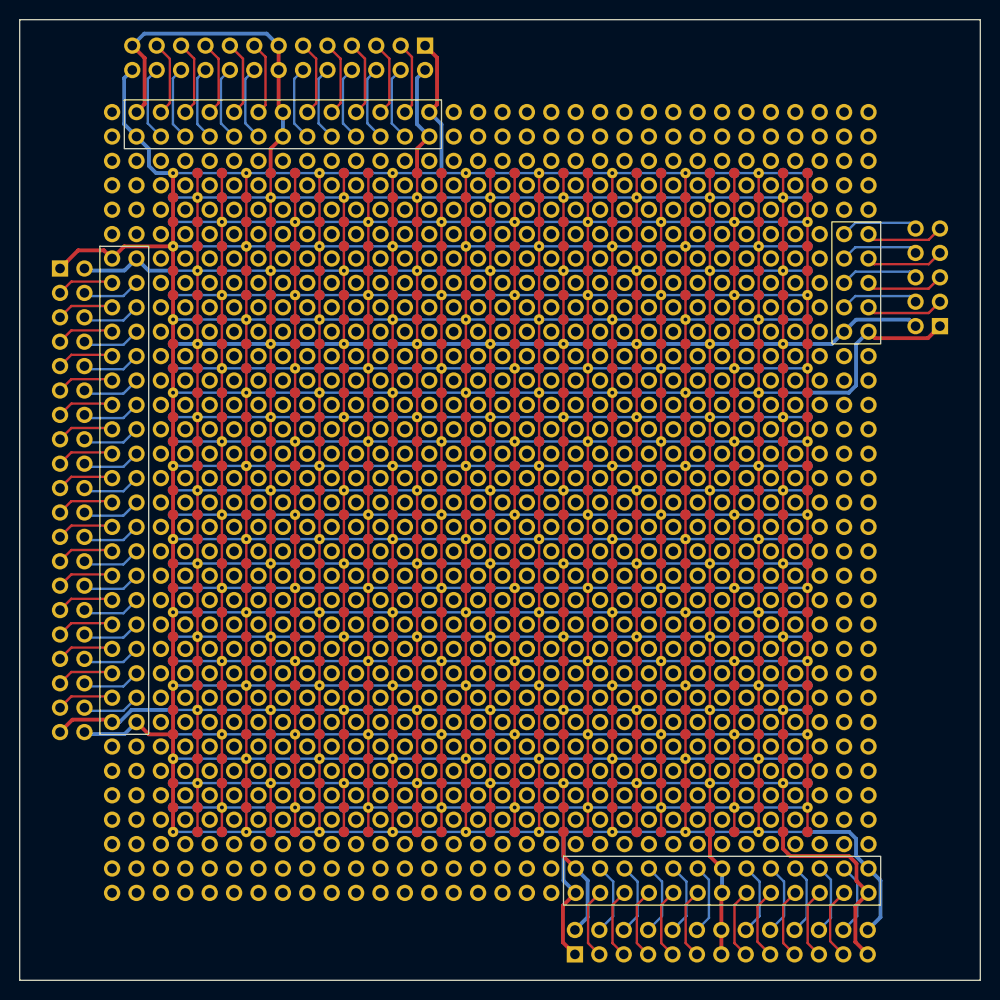
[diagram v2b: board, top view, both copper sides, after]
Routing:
- net +5V: track 96.3 -> 1381.1 mm
- net GND: track 128.0 -> 1343.9 mm
- net (no net): track 0.00 -> 1211.6 mm
